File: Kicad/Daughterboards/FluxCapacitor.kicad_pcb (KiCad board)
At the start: 2 copper layers, 100.5 x 100 mm, 56 parts, among them J10 RELAY, J13 RJ45, J14 Conn_01x03_Socket, J15 Conn_01x03_Socket, J19 JST_PH_01x03_Socket, J20 JST_PH_01x03_Socket, J21 JST_PH_01x03_Socket, J22 JST_PH_01x03_Socket, J23 JST_PH_01x03_Socket, J4 TREADMILL_CTRL_PANEL1, K1 G5V-1, Q1 2N7000, SW1 SW_SPDT_321, SW7 SW_Push_Open_Dual, SW8 SW_Push_Open_Dual, SW9 SW_Push_Open_Dual, U3 DRV5033AJxLPG, U6 SMF5.0A-T13

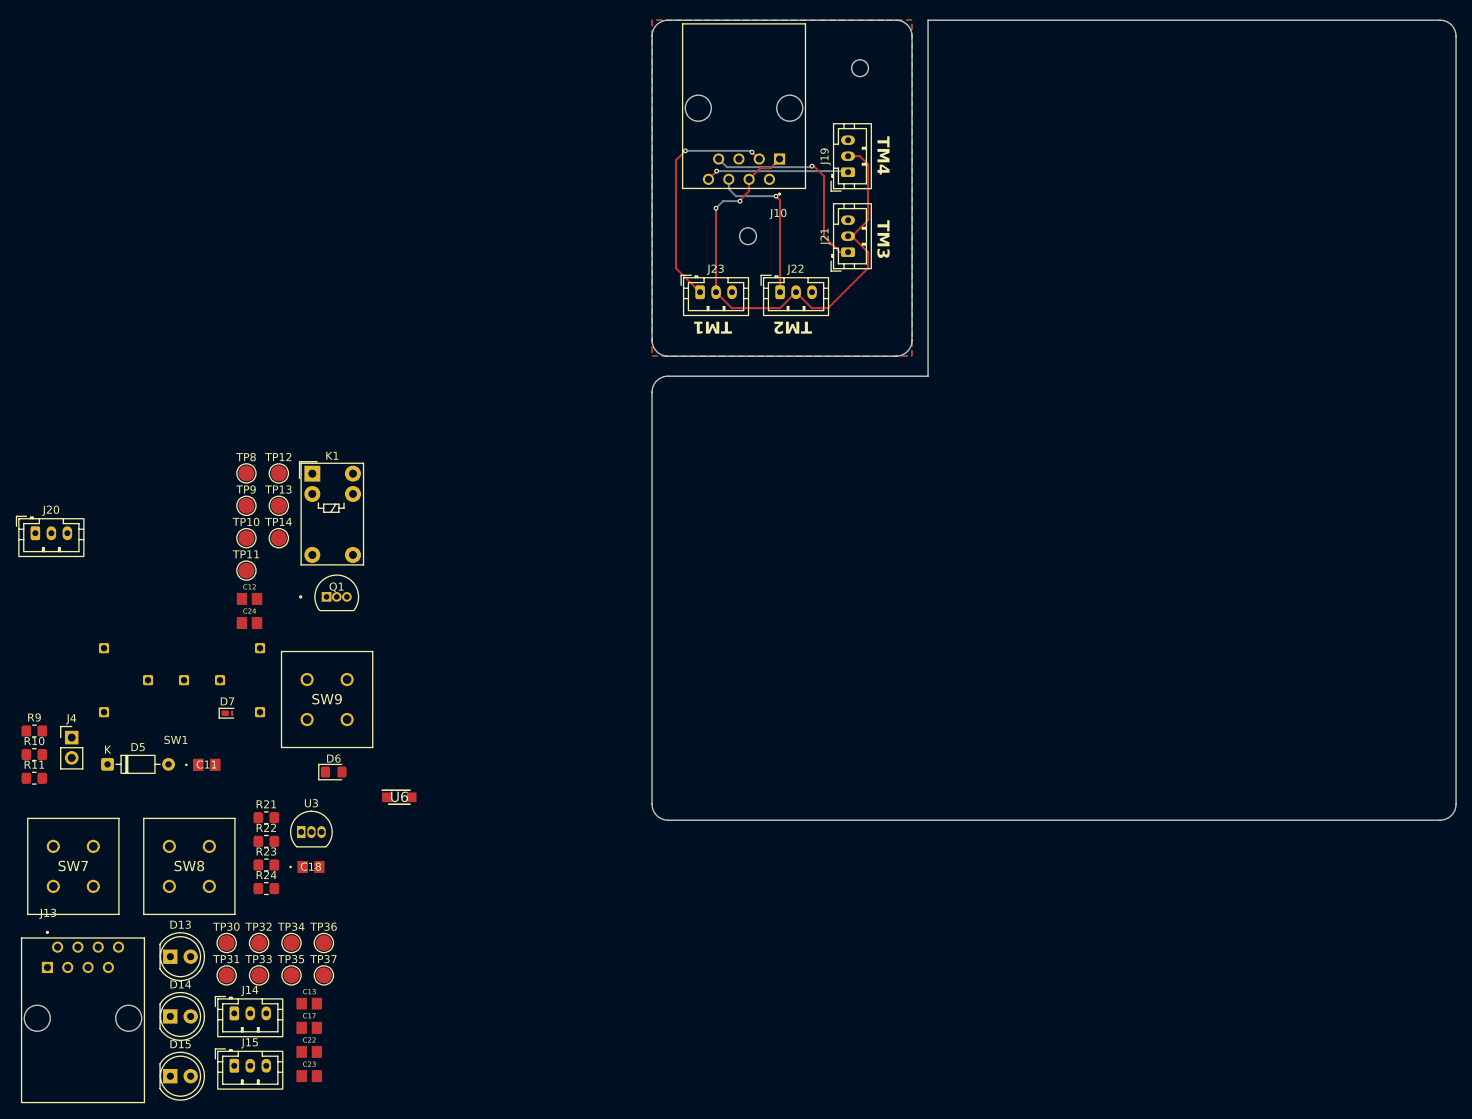
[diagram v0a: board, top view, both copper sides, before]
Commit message: Finished project
Made daughterboard pcbs, fixed silkscreen errors on mainboard pcb, generated GERBERs and drill files
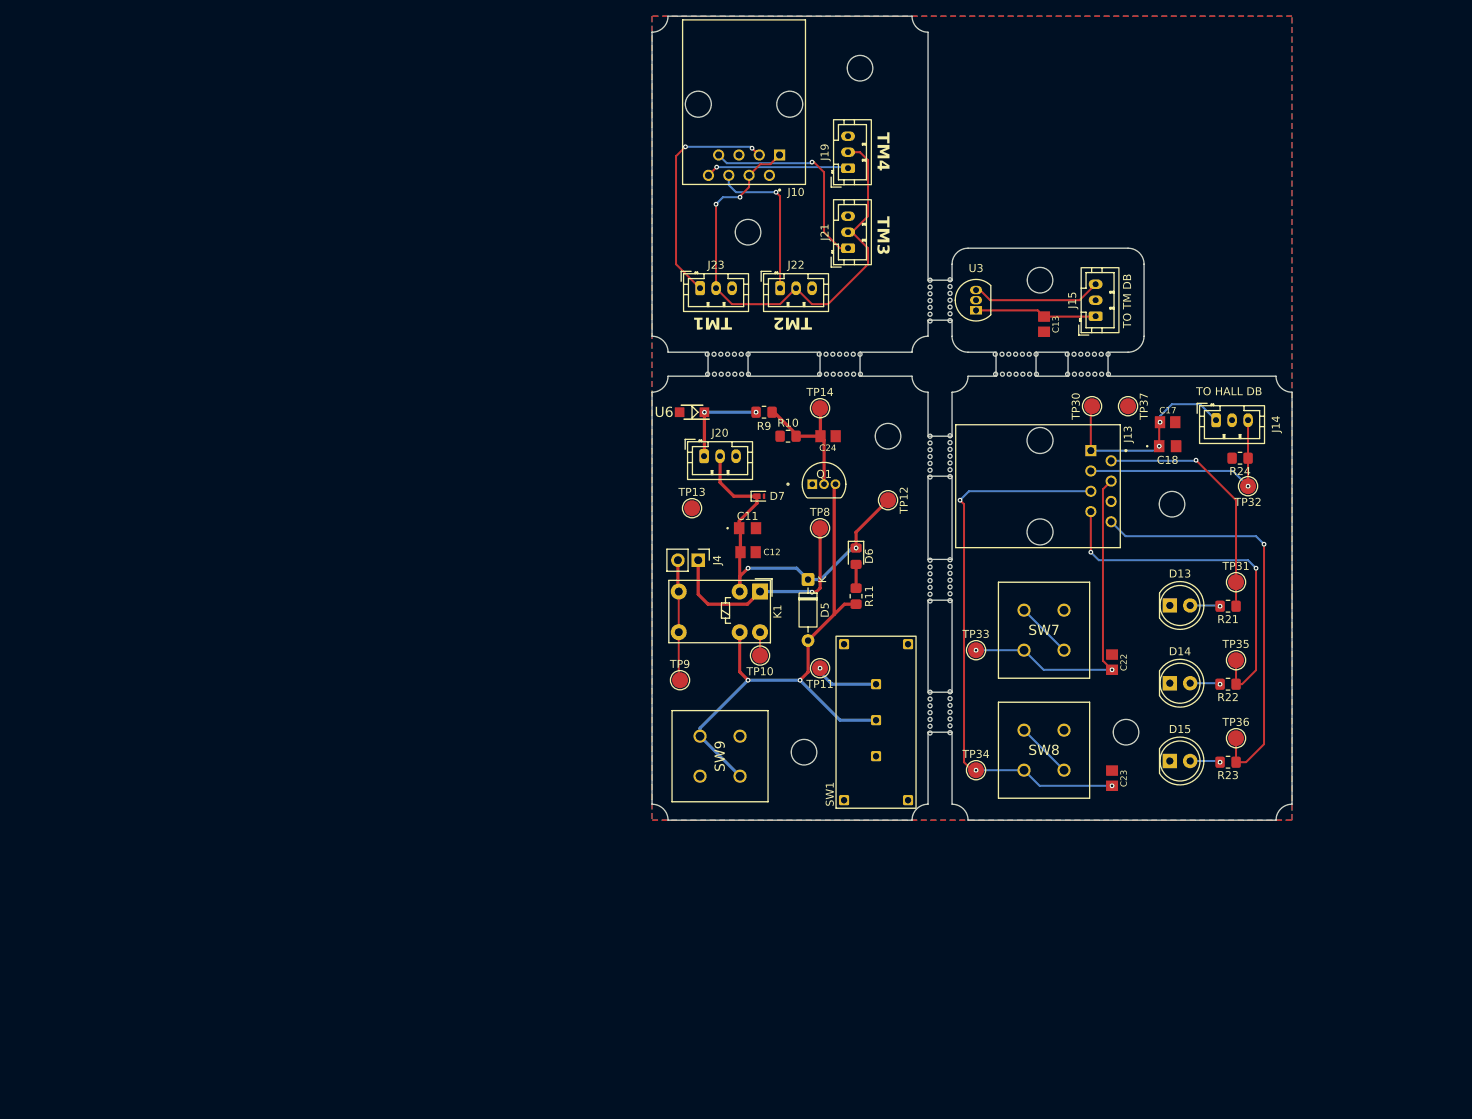
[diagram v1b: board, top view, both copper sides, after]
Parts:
- removed the REF** at (126.0, 56.0)
- removed the REF** at (112.0, 77.0)
- added REF**: MouseBite-Part_2.0x4.5mm_inset_D0.5mm_P0.85mm_7h, Panelization:MouseBite-Part_2.0x4.5mm_inset_D0.5mm_P0.85mm_7h, F.Cu at (123.5, 94.0)
- added REF**: MountingHole_3.2mm_M3, MountingHole:MountingHole_3.2mm_M3, F.Cu at (119.0, 141.5)
- added REF**: MountingHole_3.2mm_M3, MountingHole:MountingHole_3.2mm_M3, F.Cu at (126.0, 56.0)
- added REF**: MountingHole_3.2mm_M3, MountingHole:MountingHole_3.2mm_M3, F.Cu at (165.0, 110.5)
- added REF**: MountingHole_3.2mm_M3, MountingHole:MountingHole_3.2mm_M3, F.Cu at (129.5, 102.0)
- added REF**: MouseBite-Part_2.0x4.5mm_inset_D0.5mm_P0.85mm_7h, Panelization:MouseBite-Part_2.0x4.5mm_inset_D0.5mm_P0.85mm_7h, F.Cu at (145.5, 94.0)
- added REF**: MountingHole_3.2mm_M3, MountingHole:MountingHole_3.2mm_M3, F.Cu at (112.0, 76.5)
- added REF**: MouseBite-Part_2.0x4.5mm_inset_D0.5mm_P0.85mm_7h, Panelization:MouseBite-Part_2.0x4.5mm_inset_D0.5mm_P0.85mm_7h, F.Cu at (137.0, 136.5)
- added REF**: MouseBite-Part_2.0x4.5mm_inset_D0.5mm_P0.85mm_7h, Panelization:MouseBite-Part_2.0x4.5mm_inset_D0.5mm_P0.85mm_7h, F.Cu at (109.5, 94.0)
- added REF**: MouseBite-Part_2.0x4.5mm_inset_D0.5mm_P0.85mm_7h, Panelization:MouseBite-Part_2.0x4.5mm_inset_D0.5mm_P0.85mm_7h, F.Cu at (137.0, 85.0)
- added REF**: MouseBite-Part_2.0x4.5mm_inset_D0.5mm_P0.85mm_7h, Panelization:MouseBite-Part_2.0x4.5mm_inset_D0.5mm_P0.85mm_7h, F.Cu at (137.0, 104.5)
- added REF**: MouseBite-Part_2.0x4.5mm_inset_D0.5mm_P0.85mm_7h, Panelization:MouseBite-Part_2.0x4.5mm_inset_D0.5mm_P0.85mm_7h, F.Cu at (154.5, 94.0)
- added REF**: MountingHole_3.2mm_M3, MountingHole:MountingHole_3.2mm_M3, F.Cu at (148.5, 82.5)
- added REF**: MouseBite-Part_2.0x4.5mm_inset_D0.5mm_P0.85mm_7h, Panelization:MouseBite-Part_2.0x4.5mm_inset_D0.5mm_P0.85mm_7h, F.Cu at (137.0, 120.0)
- added REF**: MountingHole_3.2mm_M3, MountingHole:MountingHole_3.2mm_M3, F.Cu at (159.2, 139.0)
- TP11: value TP_NC -> TP_SPDT_NC
- moved J14 143.4 mm to (170.5, 100.0)
- moved J15 142.7 mm to (155.4, 87.0), turned to 90 degrees
- moved J13 136.9 mm to (148.5, 108.2), turned to -90 degrees
- moved TP32 136.2 mm to (174.5, 108.2), turned to 180 degrees
- moved TP31 135.4 mm to (173.0, 120.2)
- moved R24 133.1 mm to (173.5, 104.8), turned to 180 degrees
- moved D13 132.4 mm to (164.7, 123.2)
- moved D14 131.7 mm to (164.7, 132.9)
- moved C17 131.3 mm to (164.4, 100.2)
- moved D15 131.0 mm to (164.7, 142.6)
- moved TP30 127.3 mm to (155.0, 98.2), turned to 90 degrees
- moved C13 125.1 mm to (149.0, 88.0), turned to -90 degrees
- moved SW7 124.9 mm to (146.5, 128.8)
- moved TP35 124.5 mm to (173.0, 130.0)
- moved TP37 123.2 mm to (159.5, 98.2), turned to -90 degrees
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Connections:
- J15 pad 2: Net-(J15-Pin_2) -> GND
- U3 pad 2: Net-(J15-Pin_2) -> GND
- U6 pad 1: (no net) -> /RLY_TRIGGER
- U6 pad 2: (no net) -> GND
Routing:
- net Net-(D5-A): track 0.00 -> 70.6 mm, vias 0 -> 2
- net /TM_DAUGHTERBOARD/STARTSTOP_BTN: track 0.00 -> 69.5 mm, vias 0 -> 3
- net /TM_DAUGHTERBOARD/PRESET_LED_2: track 0.00 -> 52.7 mm, vias 0 -> 1
- net RLY_12V: track 0.00 -> 48.3 mm, vias 0 -> 2
- net /TM_DAUGHTERBOARD/PRESET_LED_1: track 0.00 -> 45.5 mm, vias 0 -> 2
- net /TM_DAUGHTERBOARD/PRESET_BTN: track 0.00 -> 42.5 mm, vias 0 -> 2
- net /TM_DAUGHTERBOARD/PWR_LED: track 0.00 -> 30.4 mm, vias 0 -> 1
- net /TM_DAUGHTERBOARD/HALL_OUT: track 0.00 -> 28.9 mm, vias 0 -> 1
- net Net-(J4-Pin_1): track 0.00 -> 28.4 mm, vias 0 -> 1
- net TBD_3V3: track 0.00 -> 26.6 mm, vias 0 -> 2
- net Net-(Q1-G): track 0.00 -> 17.1 mm
- net Net-(J15-Pin_3): track 0.00 -> 15.8 mm
- net Net-(J4-Pin_2): track 0.00 -> 15.1 mm
- net Net-(J15-Pin_1): track 0.00 -> 14.8 mm
- net /RLY_TRIGGER: track 0.00 -> 12.0 mm, vias 0 -> 2
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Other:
- board size 100.5 x 100 mm -> 80 x 100.5 mm
- board text added: "TO HALL DB"
- board text added: "TO TM DB"
